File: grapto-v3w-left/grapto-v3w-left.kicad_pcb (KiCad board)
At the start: 2 copper layers, 153.9 x 128.9 mm, 117 parts

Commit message: update generated pcbs
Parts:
- removed S30, S31, S32, S33, S34, S35, S36, S37, S38, S39, S40, S41, S42, S43, S44, S45, S46, S47, S48, S49, S50, S51, S52, S53, S54, S55, S56, S57, S58, S59, S60, S61, S62, S63, S64, S65, S66, S67, S68, S69, S70, S71, S72, S73, S74, S75, S76, S77, S78, S79, S80, S81, S82, S83, S84, S85, S86, S87: , PG1350
- moved USBC1 4.51 mm to (332.5, 93.8)
- moved S116 3.29 mm to (370.6, 210.5)
- moved S29 3.29 mm to (370.6, 210.5)
- moved S113 3.20 mm to (332.5, 114.0)
- moved S26 3.20 mm to (332.5, 114.0)
- moved S115 3.15 mm to (354.2, 195.5)
- moved S28 3.15 mm to (354.2, 195.5)
- moved S114 2.95 mm to (333.6, 187.2)
- moved S27 2.95 mm to (333.6, 187.2)
- moved S112 2.92 mm to (332.5, 131.5)
- moved S25 2.92 mm to (332.5, 131.5)
- moved S109 2.83 mm to (314.0, 110.0)
- moved S22 2.83 mm to (314.0, 110.0)
- moved S111 2.69 mm to (332.5, 149.0)
- moved S24 2.69 mm to (332.5, 149.0)
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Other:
- board size 153.9 x 128.9 mm -> 150 x 127.7 mm

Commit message: schematic rewrite draft done.
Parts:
- added C1: 1u, Fuse:Fuse_0603_1608Metric_Pad1.05x0.95mm_HandSolder, F.Cu at (415.9, 119.3)
- added C10: 22u, Fuse:Fuse_0603_1608Metric_Pad1.05x0.95mm_HandSolder, F.Cu at (421.2, 111.5)
- added C14: 22u, Fuse:Fuse_0603_1608Metric_Pad1.05x0.95mm_HandSolder, F.Cu at (372.2, 134.1)
- added C16: 22u, Fuse:Fuse_0603_1608Metric_Pad1.05x0.95mm_HandSolder, F.Cu at (367.8, 134.1)
- added C17: 22u, Fuse:Fuse_0603_1608Metric_Pad1.05x0.95mm_HandSolder, F.Cu at (401.8, 111.5)
- added C5: .1u, Capacitor_SMD:C_0603_1608Metric_Pad1.08x0.95mm_HandSolder, F.Cu at (411.1, 122.9)
- added D1: ~, Diode_SMD:D_SOD-123, F.Cu at (357.0, 144.1)
- added D10: ~, Diode_SMD:D_SOD-123, F.Cu at (374.2, 144.1)
- added D11: ~, Diode_SMD:D_SOD-123, F.Cu at (374.2, 150.8)
- added D12: ~, Diode_SMD:D_SOD-123, F.Cu at (357.0, 157.4)
- added D13: ~, Diode_SMD:D_SOD-123, F.Cu at (385.8, 144.1)
- added D14: ~, Diode_SMD:D_SOD-123, F.Cu at (368.5, 150.8)
- added D15: ~, Diode_SMD:D_SOD-123, F.Cu at (380.0, 147.4)
- added D16: ~, Diode_SMD:D_SOD-123, F.Cu at (380.0, 144.1)
- added D17: ~, Diode_SMD:D_SOD-123, F.Cu at (374.2, 147.4)
- added D18: ~, Diode_SMD:D_SOD-123, F.Cu at (368.5, 147.4)
- added D19: ~, Diode_SMD:D_SOD-123, F.Cu at (362.8, 157.4)
- added D2: ~, Diode_SMD:D_SOD-123, F.Cu at (374.2, 160.8)
- added D20: ~, Diode_SMD:D_SOD-123, F.Cu at (362.8, 144.1)
- added D21: ~, Diode_SMD:D_SOD-123, F.Cu at (374.2, 157.4)
- added D22: ~, Diode_SMD:D_SOD-123, F.Cu at (357.0, 154.1)
- added D23: ~, Diode_SMD:D_SOD-123, F.Cu at (357.0, 150.8)
- added D24: ~, Diode_SMD:D_SOD-123, F.Cu at (374.2, 154.1)
- added D25: ~, Diode_SMD:D_SOD-123, F.Cu at (357.0, 160.8)
- added D26: ~, Diode_SMD:D_SOD-123, F.Cu at (368.5, 154.1)
- added D27: ~, Diode_SMD:D_SOD-123, F.Cu at (380.0, 150.8)
- added D28: ~, Diode_SMD:D_SOD-123, F.Cu at (385.8, 147.4)
- added D29: ~, Diode_SMD:D_SOD-123, F.Cu at (362.8, 160.8)
- added D3: ~, Diode_SMD:D_SOD-123, F.Cu at (368.5, 160.8)
- added D30: LED, LED_SMD:LED_0805_2012Metric_Pad1.15x1.40mm_HandSolder, F.Cu at (356.5, 136.5)
- added D31: LED, LED_SMD:LED_0805_2012Metric_Pad1.15x1.40mm_HandSolder, F.Cu at (411.3, 120.1)
- added D32: LED, LED_SMD:LED_0805_2012Metric_Pad1.15x1.40mm_HandSolder, F.Cu at (411.3, 117.1)
- added D33: LED, LED_SMD:LED_0805_2012Metric_Pad1.15x1.40mm_HandSolder, F.Cu at (416.6, 111.8)
- added D4: ~, Diode_SMD:D_SOD-123, F.Cu at (362.8, 147.4)
- added D5: ~, Diode_SMD:D_SOD-123, F.Cu at (368.5, 157.4)
- added D6: ~, Diode_SMD:D_SOD-123, F.Cu at (357.0, 147.4)
- added D7: ~, Diode_SMD:D_SOD-123, F.Cu at (362.8, 154.1)
- added D8: ~, Diode_SMD:D_SOD-123, F.Cu at (368.5, 144.1)
- added D9: ~, Diode_SMD:D_SOD-123, F.Cu at (362.8, 150.8)
- added F3: Polyfuse, Fuse:Fuse_0603_1608Metric_Pad1.05x0.95mm_HandSolder, F.Cu at (425.5, 114.0)
- added F4: Polyfuse, Fuse:Fuse_0603_1608Metric_Pad1.05x0.95mm_HandSolder, F.Cu at (397.4, 111.5)
- added J1: Conn_01x02_Female, Connector_JST:JST_PH_S2B-PH-SM4-TB_1x02-1MP_P2.00mm_Horizontal, F.Cu at (382.4, 133.2)
- added J6: USB_C_Receptacle_USB2.0, grapto-v3w:USB_C_Receptacle_molex_2169900001, F.Cu at (332.5, 91.6)
- added J8: Conn_01x06_Male, Connector_PinHeader_2.54mm:PinHeader_1x06_P2.54mm_Vertical, F.Cu at (379.6, 112.6)
- added JP4: SolderJumper_2_Bridged, Jumper:SolderJumper-2_P1.3mm_Bridged_RoundedPad1.0x1.5mm, F.Cu at (420.2, 119.6)
- added JP5: SolderJumper_2_Bridged, Jumper:SolderJumper-2_P1.3mm_Bridged_RoundedPad1.0x1.5mm, F.Cu at (397.4, 114.5)
- added JP6: SolderJumper_2_Bridged, Jumper:SolderJumper-2_P1.3mm_Bridged_RoundedPad1.0x1.5mm, F.Cu at (361.1, 136.8)
- added L2: 2.2, grapto-v3w:Bourns-SRP0415, F.Cu at (357.4, 132.7)
- added R1: 5.6, Resistor_SMD:R_0603_1608Metric_Pad0.98x0.95mm_HandSolder, F.Cu at (369.8, 136.6)
- added R19: 1M, Resistor_SMD:R_0603_1608Metric_Pad0.98x0.95mm_HandSolder, F.Cu at (415.9, 116.8)
- added R2: 60, Resistor_SMD:R_0603_1608Metric_Pad0.98x0.95mm_HandSolder, F.Cu at (415.4, 125.4)
- added R20: 5.1k, Resistor_SMD:R_0603_1608Metric_Pad0.98x0.95mm_HandSolder, F.Cu at (367.8, 131.6)
- added R23: 5.1k, Resistor_SMD:R_0603_1608Metric_Pad0.98x0.95mm_HandSolder, F.Cu at (365.4, 136.6)
- added R24: 22, Resistor_SMD:R_0603_1608Metric_Pad0.98x0.95mm_HandSolder, F.Cu at (374.1, 136.6)
- added R25: 22, Resistor_SMD:R_0603_1608Metric_Pad0.98x0.95mm_HandSolder, F.Cu at (372.2, 131.6)
- added R3: 60, Resistor_SMD:R_0603_1608Metric_Pad0.98x0.95mm_HandSolder, F.Cu at (421.2, 114.0)
- added R30: 2M, Resistor_SMD:R_0603_1608Metric_Pad0.98x0.95mm_HandSolder, F.Cu at (420.2, 116.5)
- added R4: 10K, Resistor_SMD:R_0603_1608Metric_Pad0.98x0.95mm_HandSolder, F.Cu at (425.5, 111.5)
- added R5: 60, Resistor_SMD:R_0603_1608Metric_Pad0.98x0.95mm_HandSolder, F.Cu at (424.6, 116.5)
- added R6: 5.6, Resistor_SMD:R_0603_1608Metric_Pad0.98x0.95mm_HandSolder, F.Cu at (411.1, 125.4)
- added R7: 3.3K, Resistor_SMD:R_0603_1608Metric_Pad0.98x0.95mm_HandSolder, F.Cu at (415.4, 122.9)
- added R8: 2.2K, Resistor_SMD:R_0603_1608Metric_Pad0.98x0.95mm_HandSolder, F.Cu at (411.1, 127.9)
- added U1: ACN52840, grapto-v3w:ACN52840, F.Cu at (365.7, 119.7)
- added U11: USBLC6-4SC6, Package_TO_SOT_SMD:SOT-23-6, F.Cu at (384.4, 125.0)
- added U14: LM3676SD-3.3, Package_SON:WSON-8-1EP_3x3mm_P0.5mm_EP1.6x2.0mm, F.Cu at (363.2, 132.6)
- added U2: BQ24073RGT, Package_DFN_QFN:VQFN-16-1EP_3x3mm_P0.5mm_EP1.6x1.6mm, F.Cu at (411.6, 112.9)

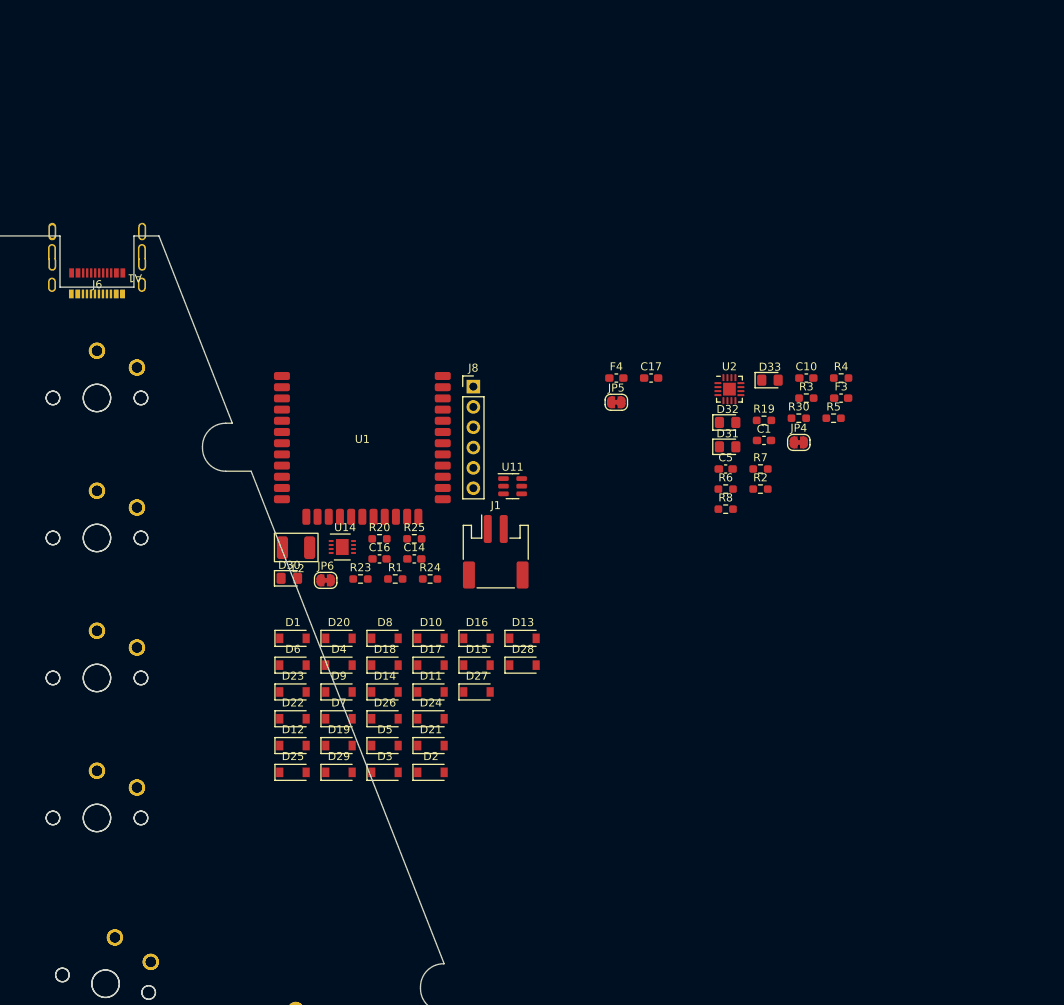
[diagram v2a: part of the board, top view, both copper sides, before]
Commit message: Added footprints.
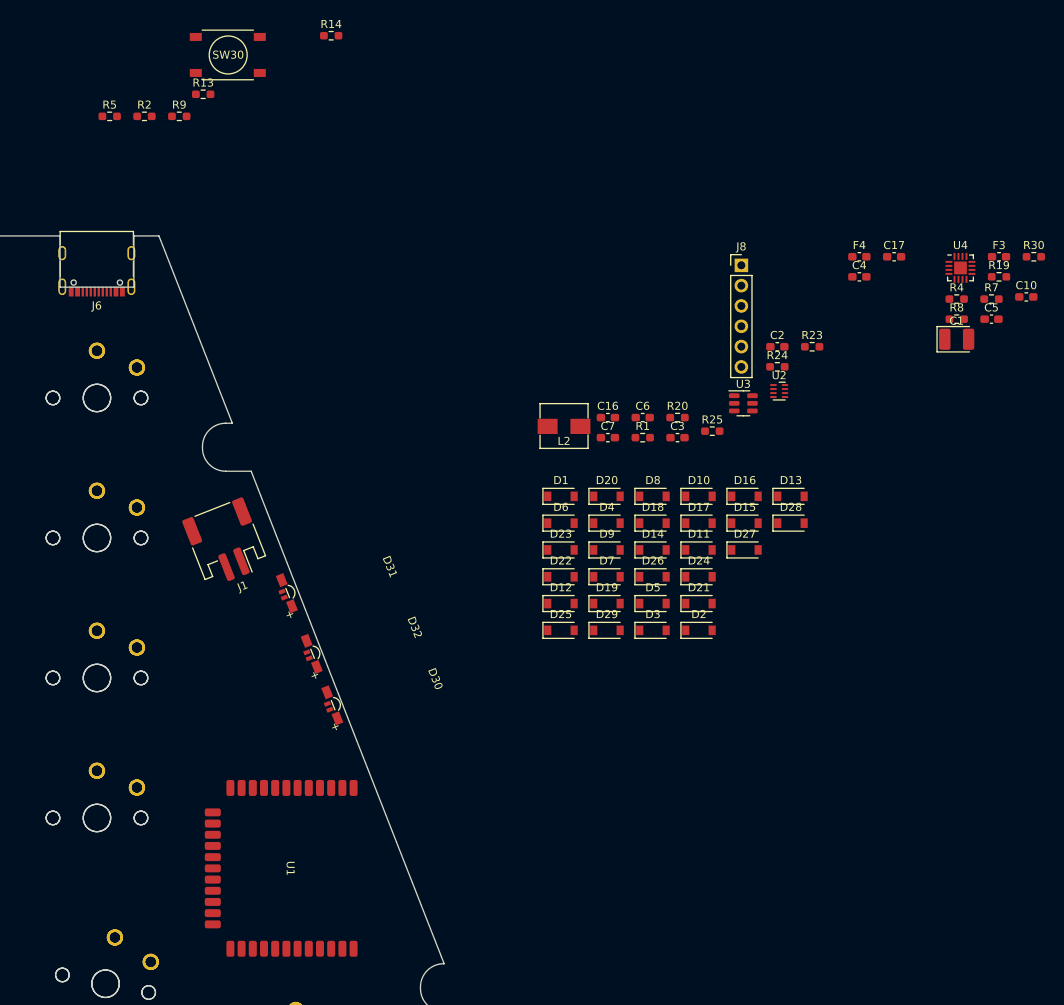
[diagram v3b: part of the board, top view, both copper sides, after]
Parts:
- removed C14: 22u, Fuse:Fuse_0603_1608Metric_Pad1.05x0.95mm_HandSolder
- removed D33: LED, LED_SMD:LED_0805_2012Metric_Pad1.15x1.40mm_HandSolder
- removed JP4, JP5, JP6: SolderJumper_2_Bridged, Jumper:SolderJumper-2_P1.3mm_Bridged_RoundedPad1.0x1.5mm
- removed R3: 60, Resistor_SMD:R_0603_1608Metric_Pad0.98x0.95mm_HandSolder
- removed R6: 5.6, Resistor_SMD:R_0603_1608Metric_Pad0.98x0.95mm_HandSolder
- removed U11: USBLC6-4SC6, Package_TO_SOT_SMD:SOT-23-6
- removed U14: LM3676SD-3.3, Package_SON:WSON-8-1EP_3x3mm_P0.5mm_EP1.6x2.0mm
- removed USBC1: TRRS-PJ-320A-dual, TRRS-PJ-320A-dual
- added C2: 120p, Fuse:Fuse_0603_1608Metric_Pad1.05x0.95mm_HandSolder, F.Cu at (417.6, 107.6)
- added C3: 22u, Fuse:Fuse_0603_1608Metric_Pad1.05x0.95mm_HandSolder, F.Cu at (405.1, 119.0)
- added C4: 22u, Fuse:Fuse_0603_1608Metric_Pad1.05x0.95mm_HandSolder, F.Cu at (427.8, 98.9)
- added C6: 22u, Fuse:Fuse_0603_1608Metric_Pad1.05x0.95mm_HandSolder, F.Cu at (400.7, 116.5)
- added C7: 22u, Fuse:Fuse_0603_1608Metric_Pad1.05x0.95mm_HandSolder, F.Cu at (396.4, 119.0)
- added R13: 0.01m, Resistor_SMD:R_0603_1608Metric_Pad0.98x0.95mm_HandSolder, F.Cu at (345.8, 76.0)
- added R14: 0.01m, Resistor_SMD:R_0603_1608Metric_Pad0.98x0.95mm_HandSolder, F.Cu at (361.8, 68.7)
- added R9: 100k, Resistor_SMD:R_0603_1608Metric_Pad0.98x0.95mm_HandSolder, F.Cu at (342.8, 78.8)
- added SW30: SW_Push_Dual, grapto-v3w:korean k2 1157sp, F.Cu at (348.9, 71.1)
- added U3: USBLC6-2SC6, Package_TO_SOT_SMD:SOT-23-6, F.Cu at (413.3, 114.7)
- added U4: BQ24074RGT, Package_DFN_QFN:VQFN-16-1EP_3x3mm_P0.5mm_EP1.6x1.6mm, F.Cu at (440.4, 97.7)
- C1: footprint Fuse:Fuse_0603_1608Metric_Pad1.05x0.95mm_HandSolder -> LED_SMD:LED_1210_3225Metric_Pad1.42x2.65mm_HandSolder
- D30, D31, D32: value LED -> LED_RGBA; footprint LED_SMD:LED_0805_2012Metric_Pad1.15x1.40mm_HandSolder -> grapto-v3w:LTST-S310F3WT
- J6: footprint grapto-v3w:USB_C_Receptacle_molex_2169900001 -> Connector_USB:USB_C_Receptacle_G-Switch_GT-USB-7010ASV
- L2: value 2.2 -> 470n; footprint grapto-v3w:Bourns-SRP0415 -> grapto-v3w:MHCI05020-R47M-R8
- R1: value 5.6 -> 62
- R2: value 60 -> 0.01m
- R5: value 60 -> 453k
- U2: value BQ24073RGT -> TPS62822DLC; footprint Package_DFN_QFN:VQFN-16-1EP_3x3mm_P0.5mm_EP1.6x1.6mm -> Package_DFN_QFN:Texas_VSON-HR-8_1.5x2mm_P0.5mm
- moved R5 98.0 mm to (334.1, 78.8)
- moved R2 90.0 mm to (338.4, 78.8)
- moved R23 63.5 mm to (421.9, 107.6)
- moved D32 59.5 mm to (359.4, 146.0), turned to -68.5 degrees
- moved D31 58.1 mm to (356.2, 138.4), turned to -68.5 degrees
- moved U1 54.0 mm to (356.2, 172.8), turned to -90 degrees
- moved R24 50.9 mm to (417.6, 110.1)
- moved R20 40.2 mm to (405.1, 116.5)
- moved R25 39.6 mm to (409.4, 118.2)
- moved C5 38.1 mm to (444.3, 104.2)
- moved D1 37.9 mm to (390.5, 126.3)
- moved D10 37.9 mm to (407.8, 126.3)
- moved D13 37.9 mm to (419.2, 126.3)
- moved D16 37.9 mm to (413.5, 126.3)
- moved D20 37.9 mm to (396.2, 126.3)
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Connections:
- D30 pad 1: sysgnd -> Net-(D30-Pad1)
- D30 pad 2: Net-(D30-Pad2) -> /controller/chg_led
- D31 pad 1: Net-(D31-Pad1) -> unconnected-(D31-Pad1)
- D31 pad 2: Net-(D31-Pad2) -> /controller/bat_lvl1
- D32 pad 1: Net-(D32-Pad1) -> unconnected-(D32-Pad1)
- D32 pad 2: Net-(D32-Pad2) -> /controller/status1
- J8 pad 6: /controller/3.3v -> /controller/vdd
- R1 pad 1: /controller/status -> /controller/fast_chg_led
- R1 pad 2: Net-(D30-Pad2) -> Net-(D30-Pad1)
- R2 pad 1: /controller/vsys -> Net-(C17-Pad1)
- R2 pad 2: Net-(R2-Pad2) -> /controller/vdd
- R5 pad 1: Net-(R2-Pad2) -> Net-(C17-Pad1)
- R5 pad 2: Net-(D32-Pad2) -> Net-(C2-Pad2)
- U1 pad 12: /controller/3.3v -> /controller/vdd
- U1 pad 24: /controller/3.3v -> /controller/vdd
- U1 pad 3: sysgnd -> /controller/fast_chg_led
- U1 pad 32: /controller/3.3v -> /controller/vdd
- U1 pad 4: sysgnd -> /controller/bat_lvl1
- U1 pad 5: sysgnd -> /controller/bat_lvl2
- U1 pad 6: sysgnd -> /controller/status1
- U1 pad 7: sysgnd -> /controller/status2
- U1 pad 8: /controller/status -> sysgnd
- U2 pad 1: Net-(R4-Pad1) -> /controller/vsys
- U2 pad 2: /controller/BatteryManagement/bat_fused -> Net-(C2-Pad2)
- U2 pad 3: /controller/BatteryManagement/bat_fused -> sysgnd
- U2 pad 4: sysgnd -> unconnected-(U2-Pad4)
- U2 pad 5: /controller/fast_chg -> sysgnd
- U2 pad 6: sysgnd -> Net-(L2-Pad1)
- U2 pad 7: Net-(D32-Pad1) -> /controller/vsys
- U2 pad 8: sysgnd -> unconnected-(U2-Pad8)

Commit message: before adding hotswaps
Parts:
- C1: footprint LED_SMD:LED_1210_3225Metric_Pad1.42x2.65mm_HandSolder -> Capacitor_SMD:C_0603_1608Metric_Pad1.08x0.95mm_HandSolder
- D30, D31, D32: value LED_RGBA -> LED_ARGB; footprint grapto-v3w:LTST-S310F3WT -> grapto-v3w:23-23B-R6GHBHC-A01-2A
- moved C1 99.6 mm to (340.5, 100.7), turned to -90 degrees
- moved F4 93.2 mm to (335.0, 105.0)
- moved R23 90.8 mm to (331.1, 104.8), turned to 90 degrees
- moved SW30 78.1 mm to (346.2, 149.1)
- moved R20 77.1 mm to (328.6, 106.3), turned to 90 degrees
- moved U2 75.8 mm to (342.3, 119.5)
- moved U3 74.0 mm to (339.9, 104.9)
- moved R24 73.2 mm to (344.4, 106.8)
- moved R25 66.7 mm to (343.2, 110.2)
- moved R13 37.7 mm to (342.0, 113.6)
- moved D30 5.51 mm to (356.4, 152.1), turned to 90 degrees
- moved D32 2.91 mm to (356.5, 145.3), turned to 90 degrees
- turned D31 to 90 degrees
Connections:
- D30 pad 1: Net-(D30-Pad1) -> /controller/vdd
- D30 pad 2: /controller/chg_led -> Net-(R1-Pad2)
- D30 pad 3: unconnected-(D30-Pad3) -> /controller/chg_led
- D30 pad 4: /controller/vdd -> unconnected-(D30-Pad4)
- D31 pad 1: unconnected-(D31-Pad1) -> /controller/vdd
- D31 pad 2: /controller/bat_lvl1 -> unconnected-(D31-Pad2)
- D31 pad 3: /controller/bat_lvl2 -> /controller/bat_lvl1
- D31 pad 4: /controller/vdd -> /controller/bat_lvl2
- D32 pad 1: unconnected-(D32-Pad1) -> /controller/vdd
- D32 pad 2: /controller/status1 -> unconnected-(D32-Pad2)
- D32 pad 3: /controller/status2 -> /controller/status1
- D32 pad 4: /controller/vdd -> /controller/status2
- R1 pad 2: Net-(D30-Pad1) -> Net-(R1-Pad2)

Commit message: left half pcb draft.
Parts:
- removed D1, D10, D11, D12, D13, D14, D15, D16, D17, D18, D19, D2, D20, D21, D22, D23, D24, D25, D26, D27, D28, D29, D3, D4, D5, D6, D7, D8, D9: ~, Diode_SMD:D_SOD-123
- removed SW30: SW_Push_Dual, grapto-v3w:korean k2 1157sp
- added D100: , ComboDiode, F.Cu at (295.5, 179.5)
- added D101: , ComboDiode, F.Cu at (295.5, 162.0)
- added D102: , ComboDiode, F.Cu at (295.5, 144.5)
- added D103: , ComboDiode, F.Cu at (295.5, 127.0)
- added D104: , ComboDiode, F.Cu at (295.5, 109.5)
- added D105: , ComboDiode, F.Cu at (314.0, 184.5)
- added D106: , ComboDiode, F.Cu at (314.0, 167.0)
- added D107: , ComboDiode, F.Cu at (314.0, 149.5)
- added D108: , ComboDiode, F.Cu at (314.0, 132.0)
- added D109: , ComboDiode, F.Cu at (314.0, 114.5)
- added D110: , ComboDiode, F.Cu at (332.5, 171.0)
- added D111: , ComboDiode, F.Cu at (332.5, 153.5)
- added D112: , ComboDiode, F.Cu at (332.5, 136.0)
- added D113: , ComboDiode, F.Cu at (332.5, 118.5)
- added D114: , ComboDiode, F.Cu at (332.7, 191.6)
- added D115: , ComboDiode, F.Cu at (351.8, 199.3)
- added D116: , ComboDiode, F.Cu at (367.0, 213.2)
- added D88: , ComboDiode, F.Cu at (240.0, 184.5)
- added D89: , ComboDiode, F.Cu at (240.0, 167.0)
- added D90: , ComboDiode, F.Cu at (240.0, 149.5)
- added D91: , ComboDiode, F.Cu at (258.5, 184.5)
- added D92: , ComboDiode, F.Cu at (258.5, 167.0)
- added D93: , ComboDiode, F.Cu at (258.5, 149.5)
- added D94: , ComboDiode, F.Cu at (258.5, 132.0)
- added D95: , ComboDiode, F.Cu at (277.0, 184.5)
- added D96: , ComboDiode, F.Cu at (277.0, 167.0)
- added D97: , ComboDiode, F.Cu at (277.0, 149.5)
- added D98: , ComboDiode, F.Cu at (277.0, 132.0)
- added D99: , ComboDiode, F.Cu at (277.0, 114.5)
- added SW31: SW_SPDT, grapto-v3w:SW_SK-3296S-01-L2, B.Cu at (347.1, 115.4)
- added TP1: TestPoint, Connector_PinHeader_2.54mm:PinHeader_1x01_P2.54mm_Vertical, B.Cu at (349.0, 126.0)
- added TP10: TestPoint, Connector_PinHeader_2.54mm:PinHeader_1x01_P2.54mm_Vertical, B.Cu at (356.8, 138.9)
- added TP11: TestPoint, Connector_PinHeader_2.54mm:PinHeader_1x01_P2.54mm_Vertical, B.Cu at (361.3, 148.0)
- added TP13: TestPoint, Connector_PinHeader_2.54mm:PinHeader_1x01_P2.54mm_Vertical, B.Cu at (340.5, 100.6)
- added TP14: TestPoint, Connector_PinHeader_2.54mm:PinHeader_1x01_P2.54mm_Vertical, B.Cu at (317.7, 101.5)
- added TP15: TestPoint, Connector_PinHeader_2.54mm:PinHeader_1x01_P2.54mm_Vertical, B.Cu at (317.6, 97.0)
- added TP16: TestPoint, Connector_PinHeader_2.54mm:PinHeader_1x01_P2.54mm_Vertical, B.Cu at (347.7, 145.8)
- added TP17: TestPoint, Connector_PinHeader_2.54mm:PinHeader_1x01_P2.54mm_Vertical, B.Cu at (360.9, 155.5)
- added TP18: TestPoint, Connector_PinHeader_2.54mm:PinHeader_1x01_P2.54mm_Vertical, B.Cu at (362.3, 159.3)
- added TP22: ~, Connector_PinHeader_2.54mm:PinHeader_1x01_P2.54mm_Vertical, B.Cu at (343.9, 191.4)
- C1, C10, C16, C17, C2, C3, C4, C5, C6, C7, D30, D31, D32, F3, F4, J1, J6, J8, L2, R1, R13, R14, R2, R20, R23, R24, R25, R4, R5, R7, R8, R9, U1, U2, U3: moved to B.Cu
- R19: value 1M -> 1M2; moved to B.Cu
- R30: value 2M -> 3M; moved to B.Cu
- U4: value BQ24074RGT -> BQ24075RGT; moved to B.Cu
- moved R7 107.8 mm to (337.6, 117.1), turned to 90 degrees
- moved J8 107.1 mm to (378.2, 198.7), turned to 45 degrees
- moved R30 104.8 mm to (357.8, 146.8), turned to 180 degrees
- moved C4 104.3 mm to (343.8, 160.6), turned to 90 degrees
- moved U4 101.7 mm to (341.3, 120.3), turned to 180 degrees
- moved C10 100.1 mm to (351.6, 125.7), turned to -90 degrees
- moved F3 98.8 mm to (354.3, 135.0), turned to 90 degrees
- moved R19 97.4 mm to (357.8, 141.7)
- moved C5 95.3 mm to (357.8, 144.2), turned to 180 degrees
- moved R4 94.8 mm to (347.4, 122.3)
- moved C17 92.4 mm to (359.1, 152.9)
- moved R8 91.4 mm to (350.3, 121.9), turned to 90 degrees
- moved C6 87.4 mm to (348.9, 186.9)
- moved R2 81.3 mm to (358.2, 157.7), turned to -90 degrees
- moved C2 73.8 mm to (353.3, 144.0), turned to 180 degrees
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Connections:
- net /controller/vsys renamed vsys
- J8 pad 3: /controller/status -> /controller/status1
- R24 pad 1: usb1_n -> USB0_N
- R25 pad 1: usb1_p -> USB0_P
- S1 pad 1: col5 -> col5row3
- S10 pad 1: col3 -> col3row2
- S100 pad 1: col4 -> col4row4
- S101 pad 1: col2 -> col2row3
- S102 pad 1: col2 -> col2row2
- S103 pad 1: col2 -> col2row1
- S104 pad 1: col2 -> col2row0
- S105 pad 1: col3 -> col3row4
- S106 pad 1: col1 -> col1row3
- S107 pad 1: col1 -> col1row2
- S108 pad 1: col1 -> col1row1
- S109 pad 1: col1 -> col1row0
- S11 pad 1: col3 -> col3row1
- S110 pad 1: col0 -> col0row3
- S111 pad 1: col0 -> col0row2
- S112 pad 1: col0 -> col0row1
- S113 pad 1: col0 -> col0row0
- S114 pad 1: col2 -> col2row4
- S115 pad 1: col1 -> col1row4
- S116 pad 1: col0 -> col0row4
- S12 pad 1: col3 -> col3row0
- S13 pad 1: col4 -> col4row4
- S14 pad 1: col2 -> col2row3
- S15 pad 1: col2 -> col2row2
- S16 pad 1: col2 -> col2row1
- S17 pad 1: col2 -> col2row0
- S18 pad 1: col3 -> col3row4
- S19 pad 1: col1 -> col1row3
- S2 pad 1: col5 -> col5row2
- S20 pad 1: col1 -> col1row2
- S21 pad 1: col1 -> col1row1
- S22 pad 1: col1 -> col1row0
- S23 pad 1: col0 -> col0row3
- S24 pad 1: col0 -> col0row2
- S25 pad 1: col0 -> col0row1
- S26 pad 1: col0 -> col0row0
- S27 pad 1: col2 -> col2row4
- S28 pad 1: col1 -> col1row4
- S29 pad 1: col0 -> col0row4
- S3 pad 1: col5 -> col5row1
- S4 pad 1: col4 -> col4row3
- S5 pad 1: col4 -> col4row2
- S6 pad 1: col4 -> col4row1
- S7 pad 1: col4 -> col4row0
- S8 pad 1: col5 -> col5row4
- S88 pad 1: col5 -> col5row3
- S89 pad 1: col5 -> col5row2
- S9 pad 1: col3 -> col3row3
- S90 pad 1: col5 -> col5row1
- S91 pad 1: col4 -> col4row3
- S92 pad 1: col4 -> col4row2
- S93 pad 1: col4 -> col4row1
- S94 pad 1: col4 -> col4row0
- S95 pad 1: col5 -> col5row4
- S96 pad 1: col3 -> col3row3
- S97 pad 1: col3 -> col3row2
- S98 pad 1: col3 -> col3row1
- S99 pad 1: col3 -> col3row0
- U1 pad 10: /controller/col5 -> col5
- U1 pad 11: /controller/col4 -> col4
- U1 pad 14: /controller/col3 -> col3
- U1 pad 15: /controller/col2 -> col2
- U1 pad 16: /controller/col1 -> col1
- U1 pad 17: /controller/col0 -> col0
- U1 pad 18: /controller/row4 -> row4
- U1 pad 19: /controller/row3 -> row3
- U1 pad 20: /controller/row2 -> row2
- U1 pad 21: /controller/row1 -> row1
- U1 pad 22: /controller/row0 -> row0
- U3 pad 4: usb1_p -> USB0_P
- U3 pad 6: usb1_n -> USB0_N
- U4 pad 15: unconnected-(U4-Pad15) -> Net-(SW31-B)
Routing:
- net row1: track 0.00 -> 215.0 mm, vias 0 -> 12
- net row0: track 0.00 -> 211.4 mm, vias 0 -> 12
- net col4: track 0.00 -> 164.0 mm, vias 0 -> 4
- net col5: track 0.00 -> 161.7 mm, vias 0 -> 2
- net row2: track 0.00 -> 152.3 mm, vias 0 -> 14
- net row4: track 0.00 -> 147.6 mm, vias 0 -> 4
- net col0: track 0.00 -> 146.3 mm, vias 0 -> 10
- net col1: track 0.00 -> 142.3 mm, vias 0 -> 8
- net col3: track 0.00 -> 136.7 mm
- net row3: track 0.00 -> 135.1 mm, vias 0 -> 10
- net col2: track 0.00 -> 130.2 mm, vias 0 -> 6
- net /controller/vusb: track 0.00 -> 125.6 mm
- net /controller/vdd: track 0.00 -> 120.2 mm
- net /controller/low_batt: track 0.00 -> 115.4 mm
- net /controller/fast_chg: track 0.00 -> 109.4 mm
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- added copper zone on F.Cu, net sysgnd
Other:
- board size 150 x 127.7 mm -> 154.6 x 129.3 mm
